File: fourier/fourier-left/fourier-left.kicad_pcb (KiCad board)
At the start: 2 copper layers, 124.4 x 80.4 mm, 129 parts, among them J1 VCC, J3 RGB, J6 C6, J7 GND, U1 ProMicro, U2 TRRS

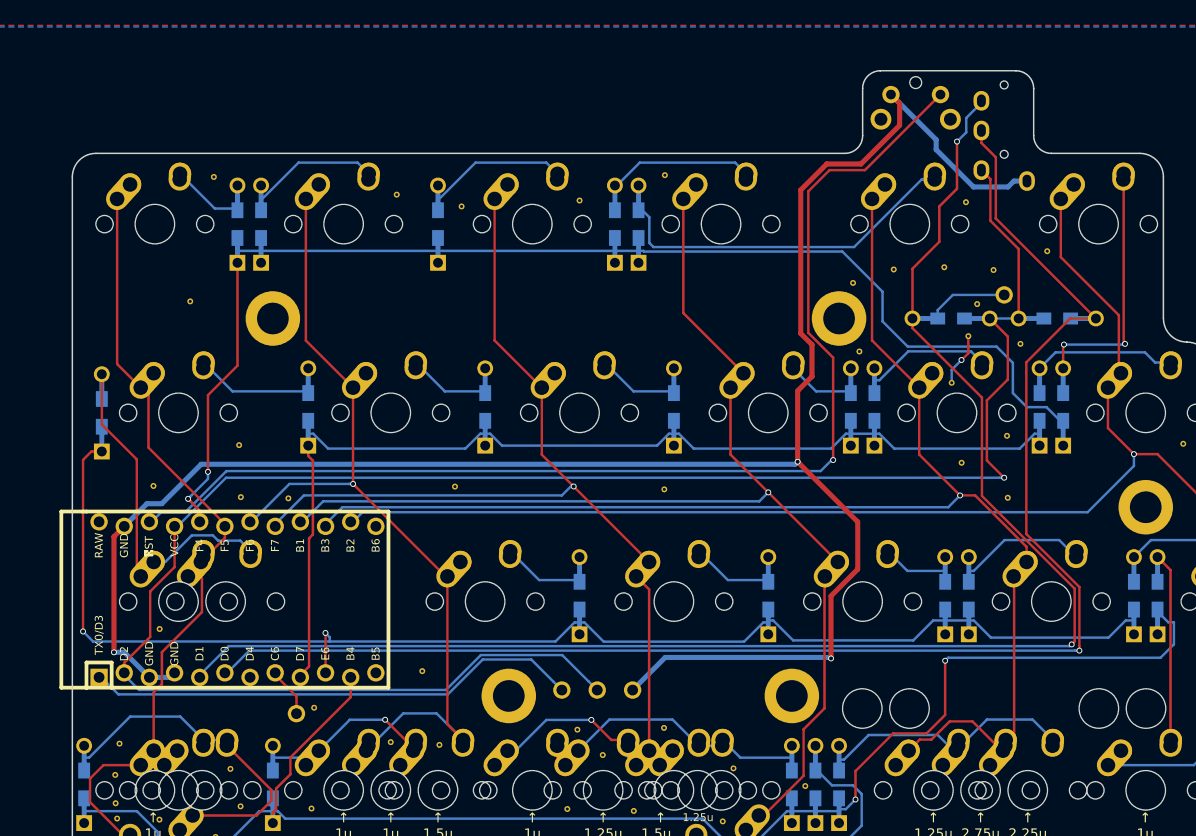
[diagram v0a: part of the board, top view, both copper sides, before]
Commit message: face controller forward and move LED breakout ports to unifrom position
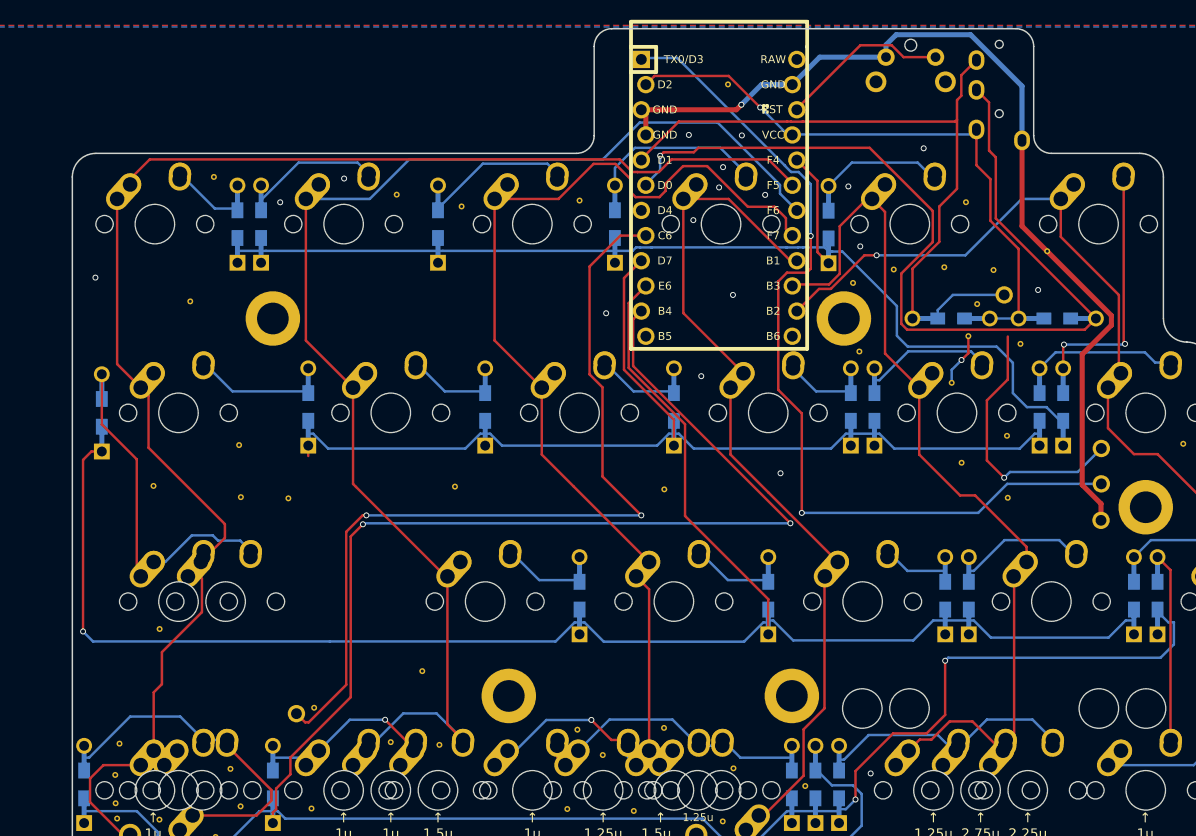
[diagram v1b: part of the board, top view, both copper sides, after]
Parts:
- removed G***: LOGO, Keebio-Art:Fourier-1.2
- removed G***: LOGO, Keebio-Art:Fourier-Sinc
- removed G***: LOGO, Keebio-Art:Keebio-TwoTone
- removed G***: LOGO, Keebio-Art:AIRI-Logo2
- moved U1 63.3 mm to (82.0, 22.4), turned to 270 degrees
- moved J3 58.3 mm to (120.5, 51.2), turned to 90 degrees
- moved J1 56.4 mm to (120.5, 47.6), turned to 90 degrees
- moved J7 50.3 mm to (120.5, 54.9), turned to 90 degrees
- moved D_A5 19.2 mm to (93.0, 25.1)
- moved REF** 11.2 mm to (82.8, 10.9)
- moved U2 4.14 mm to (110.2, 5.25)
- moved SW_RST1 3.81 mm to (103.8, 8.15)
- moved REF** 0.49 mm to (94.5, 34.5)
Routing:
- net VCC: track 192.2 -> 87.2 mm, vias 1 -> 2
- net GND: track 204.6 -> 102.1 mm, vias 4 -> 20
- net reset: track 117.2 -> 17.3 mm, vias 1 -> 0
- net data2: track 162.1 -> 70.6 mm, vias 2 -> 0
- net rowD: track 158.4 -> 245.7 mm, vias 2 -> 4
- net C6: track 4.78 -> 87.1 mm, vias 0 -> 2
- net col1: track 79.1 -> 151.6 mm
- net data: track 151.2 -> 95.0 mm
- net col6: track 155.0 -> 103.6 mm
- net col5: track 139.3 -> 88.6 mm, vias 1 -> 0
- net col2: track 85.9 -> 130.7 mm, vias 1 -> 0
- net RGB: track 50.3 -> 90.6 mm, vias 0 -> 2
- net rowC: track 140.8 -> 177.2 mm, vias 2 -> 1
- net col4: track 117.9 -> 83.6 mm, vias 1 -> 0
- net Net-(D_A5-Pad2): track 37.3 -> 12.4 mm
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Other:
- board size 124.4 x 80.4 mm -> 124.4 x 84.6 mm
- board text added: "Fourier 1.3"

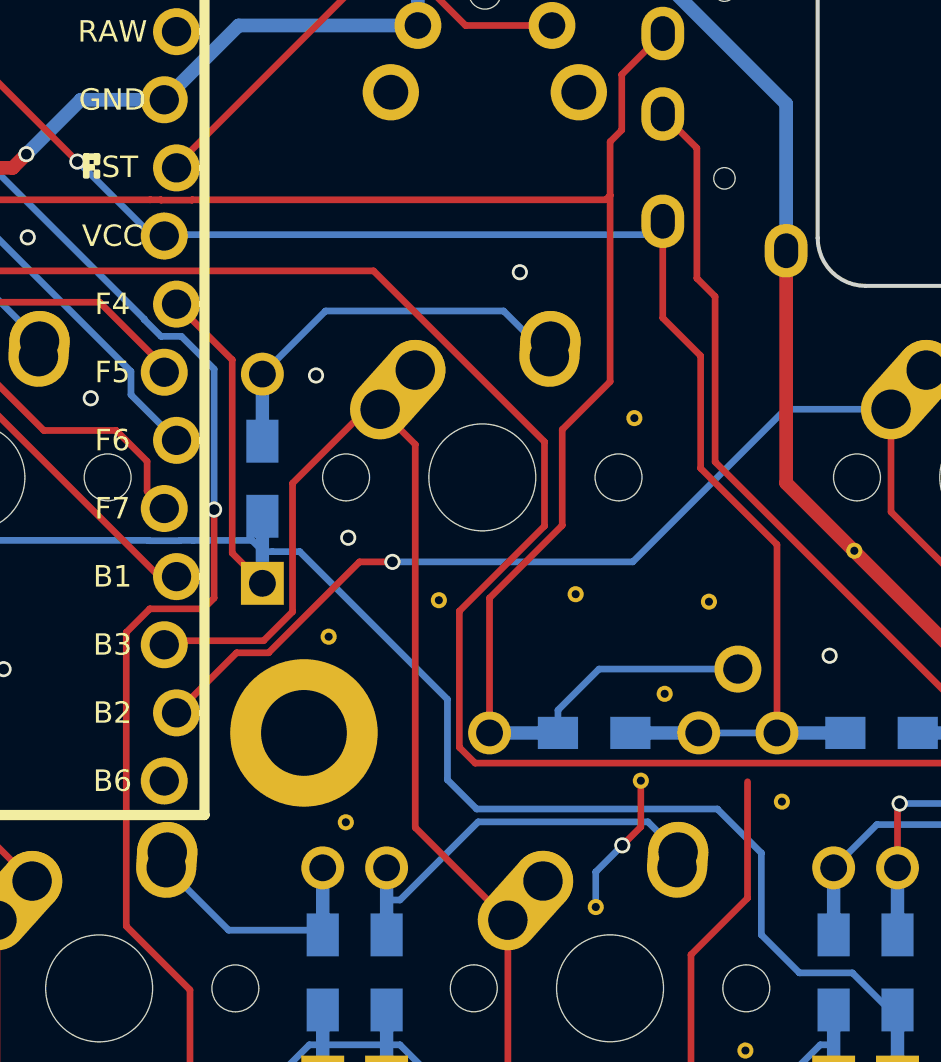
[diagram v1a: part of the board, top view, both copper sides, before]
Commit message: fixed connections and ran DRC
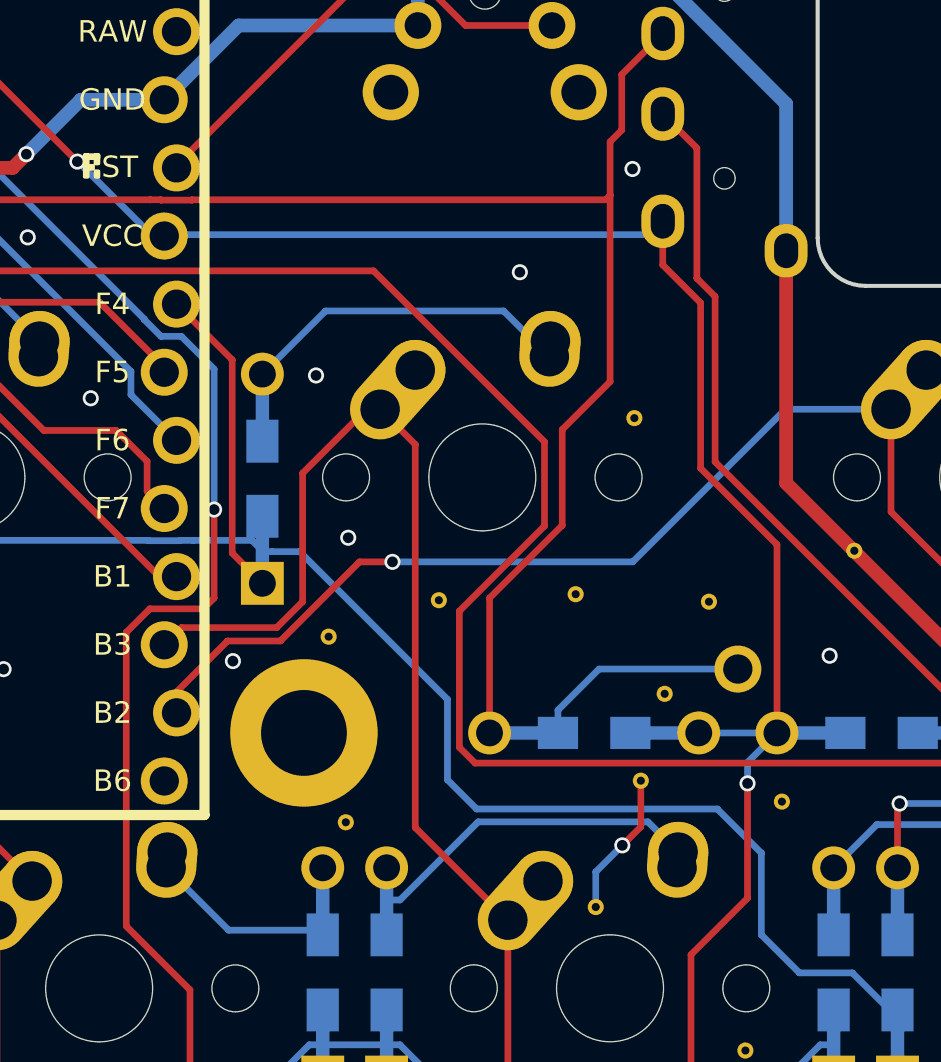
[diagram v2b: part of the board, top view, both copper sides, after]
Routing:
- net VCC: track 87.2 -> 89.6 mm, vias 2 -> 3
- net GND: vias 20 -> 22
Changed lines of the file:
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@@
     (thickness 1.6)
     (drawings 43)
-    (tracks 585)
+    (tracks 592)
     (zones 0)
     (modules 125)
@@
   (via (at 78.9 16) (size 0.6) (drill 0.4) (layers F.Cu B.Cu) (net 1))
   (via (at 97.25 80.45) (size 0.6) (drill 0.4) (layers F.Cu B.Cu) (net 1))
+  (via (at 91.9 31.85) (size 0.6) (drill 0.4) (layers F.Cu B.Cu) (net 1))
+  (via (at 106.8 13.5) (size 0.6) (drill 0.4) (layers F.Cu B.Cu) (net 1))
   (segment (start 27.54004 19.92) (end 31.048186 23.428146) (width 0.25) (layer B.Cu) (net 2))
   (segment (start 31.048186 23.428146) (end 33.337528 23.428146) (width 0.25) (layer B.Cu) (net 2))
@@
   (segment (start 97.04704 76.57) (end 104.030278 76.57) (width 0.25) (layer B.Cu) (net 23))
   (segment (start 109.270401 34.528154) (end 112.186035 34.528154) (width 0.25) (layer B.Cu) (net 24))
-  (segment (start 107.928404 19.054703) (end 107.928404 15.45) (width 0.25) (layer F.Cu) (net 24))
-  (segment (start 109.34 20.466299) (end 107.928404 19.054703) (width 0.25) (layer F.Cu) (net 24))
-  (segment (start 109.34 24.66) (end 109.34 20.466299) (width 0.25) (layer F.Cu) (net 24))
-  (segment (start 112.186035 27.506035) (end 109.34 24.66) (width 0.25) (layer F.Cu) (net 24))
-  (segment (start 112.186035 34.528154) (end 112.186035 27.506035) (width 0.25) (layer F.Cu) (net 24))
-  (segment (start 108.98 42.8) (end 111.09 40.69) (width 0.25) (layer F.Cu) (net 24))
-  (segment (start 111.09 40.69) (end 111.09 36.347753) (width 0.25) (layer F.Cu) (net 24))
-  (segment (start 108.98 48.853488) (end 108.98 42.8) (width 0.25) (layer F.Cu) (net 24))
-  (segment (start 110.728032 50.60152) (end 108.98 48.853488) (width 0.25) (layer F.Cu) (net 24))
   (via (at 110.728032 50.60152) (size 0.6) (drill 0.4) (layers F.Cu B.Cu) (net 24))
   (segment (start 89.3414 15.9) (end 89.3914 15.85) (width 0.25) (layer B.Cu) (net 24))
@@
   (segment (start 107.428404 15.95) (end 89.3914 15.95) (width 0.25) (layer B.Cu) (net 24))
   (segment (start 107.928404 15.45) (end 107.428404 15.95) (width 0.25) (layer B.Cu) (net 24))
+  (segment (start 111.09 36.41) (end 111.09 36.347753) (width 0.25) (layer F.Cu) (net 24))
+  (via (at 111.09 36.41) (size 0.6) (drill 0.4) (layers F.Cu B.Cu) (net 24))
+  (segment (start 111.09 35.624189) (end 111.09 36.41) (width 0.25) (layer B.Cu) (net 24))
+  (segment (start 112.186035 34.528154) (end 111.09 35.624189) (width 0.25) (layer B.Cu) (net 24))
+  (segment (start 110.728032 50.60152) (end 108.98 48.853488) (width 0.25) (layer F.Cu) (net 24))
+  (segment (start 108.98 48.853488) (end 108.98 42.8) (width 0.25) (layer F.Cu) (net 24))
+  (segment (start 111.09 40.69) (end 111.09 36.41) (width 0.25) (layer F.Cu) (net 24))
+  (segment (start 108.98 42.8) (end 111.09 40.69) (width 0.25) (layer F.Cu) (net 24))
+  (segment (start 107.928404 17.078404) (end 107.928404 15.45) (width 0.25) (layer F.Cu) (net 24))
+  (segment (start 109.34 18.49) (end 107.928404 17.078404) (width 0.25) (layer F.Cu) (net 24))
+  (segment (start 109.34 24.66) (end 109.34 18.49) (width 0.25) (layer F.Cu) (net 24))
+  (segment (start 112.186035 27.506035) (end 109.34 24.66) (width 0.25) (layer F.Cu) (net 24))
+  (segment (start 112.186035 34.528154) (end 112.186035 27.506035) (width 0.25) (layer F.Cu) (net 24))
   (segment (start 91.2 26.2) (end 91.2 26.2) (width 0.25) (layer B.Cu) (net 25))
   (via (at 91.2 26.2) (size 0.6) (drill 0.4) (layers F.Cu B.Cu) (net 25))
@@
   (segment (start 97.85 28.15) (end 97.85 28.15) (width 0.25) (layer B.Cu) (net 33))
   (via (at 97.85 28.15) (size 0.6) (drill 0.4) (layers F.Cu B.Cu) (net 33))
-  (segment (start 92.03859 31.54001) (end 89.7986 33.78) (width 0.25) (layer F.Cu) (net 33))
-  (segment (start 93.231402 31.54001) (end 92.03859 31.54001) (width 0.25) (layer F.Cu) (net 33))
-  (segment (start 96.621412 28.15) (end 93.231402 31.54001) (width 0.25) (layer F.Cu) (net 33))
-  (segment (start 97.85 28.15) (end 96.621412 28.15) (width 0.25) (layer F.Cu) (net 33))
   (segment (start 116.44012 26.29012) (end 116.44012 22.46) (width 0.25) (layer F.Cu) (net 33))
   (segment (start 122.3 32.15) (end 116.44012 26.29012) (width 0.25) (layer F.Cu) (net 33))
   (segment (start 122.3 39.837392) (end 122.3 32.15) (width 0.25) (layer F.Cu) (net 33))
   (segment (start 122.512624 40.050016) (end 122.3 39.837392) (width 0.25) (layer F.Cu) (net 33))
+  (segment (start 91.7 31.1) (end 89.7986 33.0014) (width 0.25) (layer F.Cu) (net 33))
+  (segment (start 93.671412 31.1) (end 91.7 31.1) (width 0.25) (layer F.Cu) (net 33))
+  (segment (start 96.621412 28.15) (end 93.671412 31.1) (width 0.25) (layer F.Cu) (net 33))
+  (segment (start 89.7986 33.0014) (end 89.7986 33.78) (width 0.25) (layer F.Cu) (net 33))
+  (segment (start 97.85 28.15) (end 96.621412 28.15) (width 0.25) (layer F.Cu) (net 33))
   (segment (start 112.987616 57.577616) (end 107.797544 52.387544) (width 0.25) (layer F.Cu) (net 34))
   (segment (start 112.987616 59.100032) (end 112.987616 57.577616) (width 0.25) (layer F.Cu) (net 34))
@@
   (segment (start 98.7 38.057408) (end 98.7 23.769896) (width 0.25) (layer F.Cu) (net 34))
   (segment (start 102.152608 41.510016) (end 98.7 38.057408) (width 0.25) (layer F.Cu) (net 34))
-  (segment (start 89.4914 31.09) (end 89.3414 31.24) (width 0.25) (layer F.Cu) (net 34))
-  (segment (start 93.045002 31.09) (end 89.4914 31.09) (width 0.25) (layer F.Cu) (net 34))
-  (segment (start 94.125001 30.010001) (end 93.045002 31.09) (width 0.25) (layer F.Cu) (net 34))
-  (segment (start 94.125001 25.219101) (end 94.125001 30.010001) (width 0.25) (layer F.Cu) (net 34))
-  (segment (start 96.884102 22.46) (end 94.125001 25.219101) (width 0.25) (layer F.Cu) (net 34))
+  (segment (start 89.9814 30.6) (end 89.3414 31.24) (width 0.25) (layer F.Cu) (net 34))
+  (segment (start 93.535002 30.6) (end 89.9814 30.6) (width 0.25) (layer F.Cu) (net 34))
+  (segment (start 94.5 29.635002) (end 93.535002 30.6) (width 0.25) (layer F.Cu) (net 34))
+  (segment (start 94.5 24.844102) (end 94.5 29.635002) (width 0.25) (layer F.Cu) (net 34))
+  (segment (start 96.884102 22.46) (end 94.5 24.844102) (width 0.25) (layer F.Cu) (net 34))
   (segment (start 97.390104 22.46) (end 96.884102 22.46) (width 0.25) (layer F.Cu) (net 34))
   (segment (start 92.59 73.886002) (end 92.59 60.597632) (width 0.25) (layer F.Cu) (net 35))

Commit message: rotate left-top and update to KiCad 5.99
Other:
- net class Default removed
- net class Power removed
